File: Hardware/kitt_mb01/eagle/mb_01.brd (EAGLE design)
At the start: 160 x 100 mm, 58 parts, among them CON1 ARDUINO_UNO, IC2.00 BQ24266RGET, P1 JST.S2B-PH-SM4-TB

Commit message: entered motor controller circuitry
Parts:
- removed C1: 470uF, rcl:SMC_P
- removed C2: 390uF, rcl:SMC_P
- removed D2: MBRS320T3, diode:SMC
- removed L1: (no value), inductor-neosid:SM-B5
- removed LED1: (no value), led:PLCC2
- removed TP1: TPSQTP19SQ, testpad:TP19SQ
- removed X1: (no value), con-phoenix-254:2POL254
- added C1.01: 22uF/25V, rcl:C1210K
- added C1.02: 100nF, rcl:C0402K
- added C1.04: XX, rcl:C0402K
- added C1.05, C1.06: 22uF/6.3V, rcl:C1206K
- added C4.01: 47uF/25V, rcl:C/6032-28R
- added C4.02: 100nF/25V, resistor:C0603K
- added C4.03: (no value), resistor:C0805K
- added C4.04, C4.05: 220nF/25V, rcl:C0603K
- added IC1: (no value), kitt.ic:HSOP8
- added IC1.01: RT8293A, kitt.ic:SOIC-8-PAD
- added L2.01: 2.6uH, rcl:POWER-CHOKE_WE-TPC
- added L4.01: BEAD, inductors:0402
- added R1.03, R1.04: XX, rcl:R0402
- added R1.05, R1.06: [0R], rcl:R0402
- added R4.01, R4.02: [0R], rcl:M0805
- added R4.03: 22kR, resistor:R0402
- added R4.04, R4.05: 1kR, resistor:R0402
- added RAILS, SOC, SOC1: (no value), con-phoenix-254:2POL254
- C1.03: value [*a]1uF -> 100nF; device rcl:C0805K -> rcl:C0402K
- L1.01: value 22uH -> BEAD; device rcl:POWER-CHOKE_WE-TPC -> inductors:0402
- L1.02: value 2.6uH -> 4.7uH
- L2: value (none) -> BEAD
- R1.01: value <1>??R -> 100kR; device rcl:R0805 -> rcl:R0402
- R1.02: value <2>??R -> XX; device rcl:R0805 -> rcl:R0402
- moved R1.02 45.1 mm to (72.4, 38.1)
- moved L1.02 42.7 mm to (89.3, 56.2), turned to 270 degrees
- moved R1.01 41.4 mm to (71.1, 40.0)
- moved R3 34.0 mm to (140.6, 20.3)
- moved C1.03 26.2 mm to (87.0, 51.4), turned to 90 degrees
- moved F1 23.8 mm to (97.1, 39.7), turned to 90 degrees
- moved R2 21.9 mm to (129.8, 21.9)
- moved D1 20.8 mm to (96.9, 30.9)
- moved L1.01 7.61 mm to (113.0, 40.8), turned to 90 degrees
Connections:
- net ARDUINO.SCL renamed SCL
- net ARDUINO.SDA renamed SDA
- net AU.!IRQ_GYRO renamed !IRQ_GYRO
- new net MOT.IN1: CON1.IO.3, IC1.3, R4.05.2
- new net MOT.IN2: CON1.IO.4, IC1.2, R4.04.2
- new net N$25: C1.04.1, IC1.01.6
- new net N$28: IC1.01.5, R1.03.1, R1.04.2
- new net N$29: C1.05.1, C1.06.1, L1.02.1, L2.1, R1.03.2
- new net N$30: C1.03.2, IC1.01.3, L1.02.2
- new net N$31: C1.03.1, IC1.01.1
- new net N$32: L2.2, R1.05.2, R1.06.1
- new net N$33: C4.04.2, C4.05.1, IC1.7, SOC1.1
- new net N$34: IC1.5, R4.02.2
- new net N$35: IC1.4, R4.03.2
- net +12V: now also C4.03.1, L4.01.2, R2.1
- net +4.1V: no longer R2.04.1
- net +5V: now also IC2.00.18, IC2.00.19, R1.05.1, R1.06.2, R2.02.2, SOC.1; no longer L2.2
- net GND: now also C1.01.2, C1.02.2, C1.05.2, C1.06.2, C4.01.-, C4.02.2, C4.03.2, C4.05.2, IC1.01.4, IC1.01.PAD, IC1.1, IC1.6, IC1.THERMAL, R1.02.1, R1.04.1, R4.01.1, R4.03.1, R4.04.1, R4.05.1, SOC.2; no longer C1.-, C1.03.2, C2.-, D2.A, R1.01.1
- net GNDA: now also RAILS.2; no longer X1.2
- net N$10: now also C4.01.+, C4.02.1, C4.04.1, IC1.8, L4.01.1; no longer LED1.C, R2.1
- net N$12: now also L2.01.2; no longer L1.02.2
- net N$18: now also L2.01.1; no longer L1.02.1
- net N$2: now also L1.01.1; no longer L1.1
- net N$3: now also C1.01.1, IC1.01.2, L1.01.2, R1.01.1; no longer C1.+, L1.2
- net N$4: now also IC1.01.7; no longer R1.02.1, TP1.TP
- net N$5: now also C1.02.1, IC1.01.8; no longer D2.C, L1.01.2
- net N$7: now also C1.04.2; no longer C2.+, L1.01.1, L2.1
- net N$9: now also R4.01.2, R4.02.1, SOC1.2; no longer IC2.00.18, IC2.00.19, R2.02.2
- net V+: now also R2.04.1
- net VCC/2: now also RAILS.1; no longer LED1.A, X1.1
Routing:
- net GND: track 84.8 -> 53.6 mm
- net N$7: track 17.3 -> 0.00 mm
- net N$5: track 16.5 -> 0.00 mm
- net VCC/2: track 13.9 -> 0.00 mm
- net +12V: track 8.39 -> 0.00 mm
- net N$3: track 6.33 -> 0.00 mm
- net N$2: track 5.61 -> 0.00 mm
- net N$4: track 5.61 -> 0.00 mm
- net RAILS.RX: track 4.36 -> 0.00 mm
- net GNDA: track 3.99 -> 0.00 mm
- net N$10: track 3.28 -> 0.00 mm
- net N$9: track 1.91 -> 0.00 mm
- net +5V: track 0.00 -> 1.91 mm
- net +4.1V: track 34.2 -> 32.5 mm
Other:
- outline, holes or cut-outs redrawn

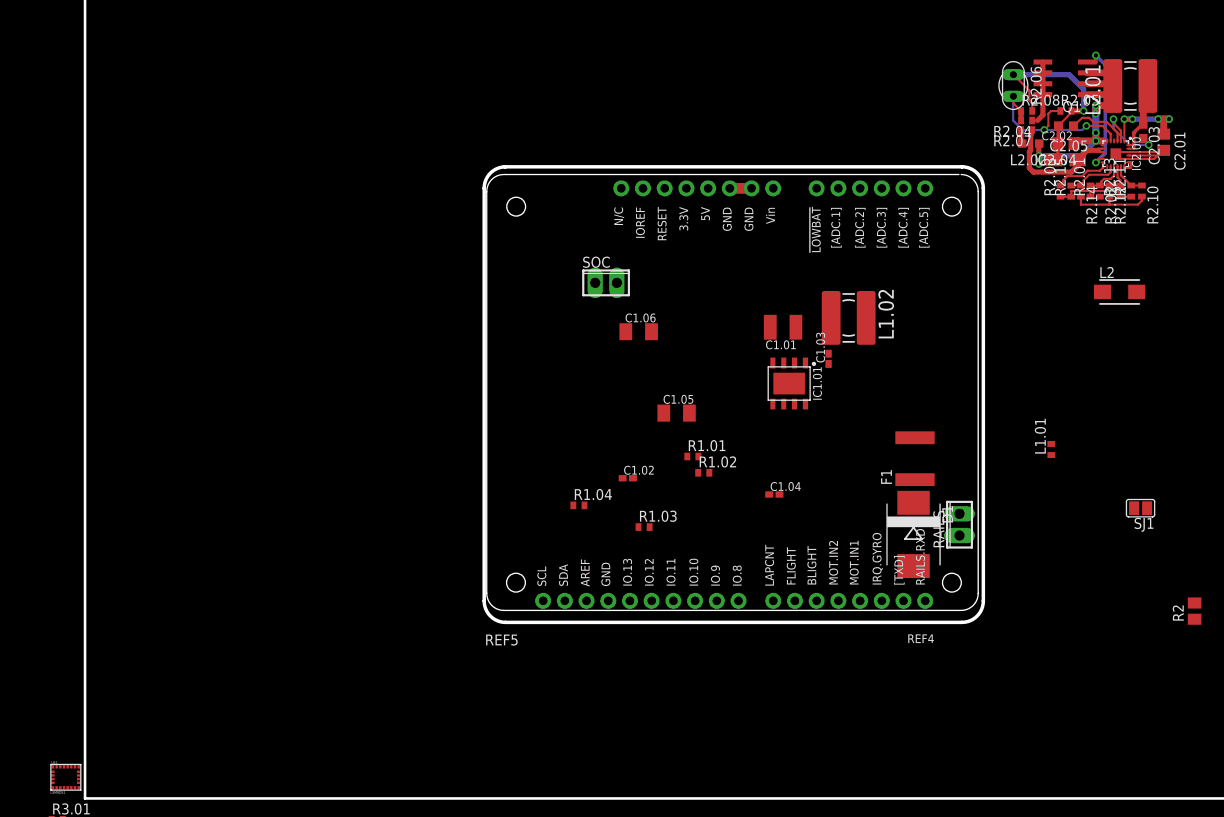
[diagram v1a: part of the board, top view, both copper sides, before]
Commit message: began working on the fullbridge
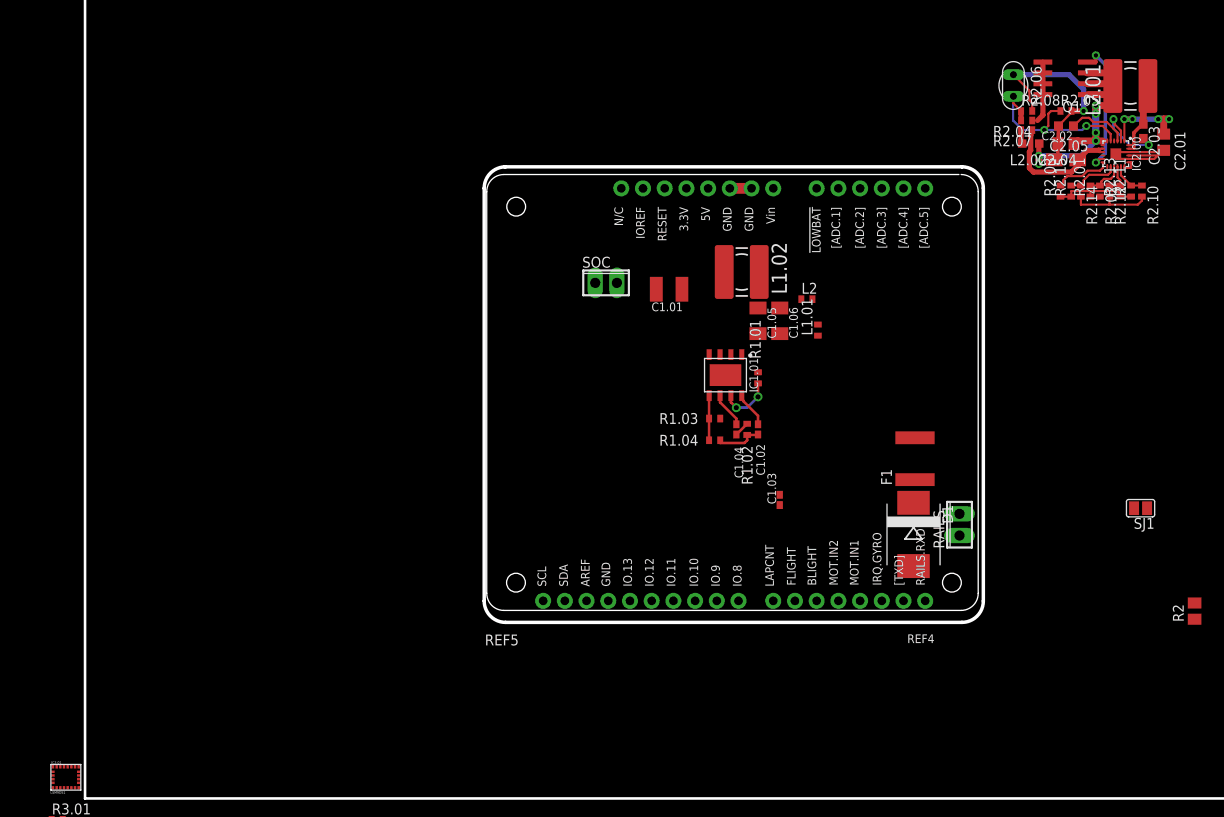
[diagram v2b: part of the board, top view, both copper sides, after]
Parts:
- L2: device inductor-neosid:SM-B5 -> inductors:0402
- moved L2 36.6 mm to (84.5, 58.4)
- moved L1.01 30.7 mm to (85.7, 54.8)
- moved R1.04 17.6 mm to (73.7, 41.9), turned to 180 degrees
- moved C1.03 17.5 mm to (81.3, 34.9)
- moved C1.06 16.6 mm to (81.3, 55.9), turned to 270 degrees
- moved C1.02 16.3 mm to (78.7, 43.2), turned to 270 degrees
- moved R1.03 15.1 mm to (73.7, 44.5)
- moved C1.05 14.4 mm to (78.7, 55.9), turned to 270 degrees
- moved C1.01 14.1 mm to (68.3, 59.6)
- moved L1.02 13.6 mm to (76.8, 61.6)
- moved R1.01 12.0 mm to (78.7, 49.2), turned to 270 degrees
- moved C1.04 8.82 mm to (76.2, 43.2), turned to 270 degrees
- moved IC1.01 7.51 mm to (74.9, 49.5)
- moved R1.02 7.18 mm to (77.5, 43.2), turned to 90 degrees
- renumbered U$1 to IC3.01
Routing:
- net N$4: track 0.00 -> 6.31 mm, vias 0 -> 2
- net GND: track 53.6 -> 59.2 mm
- net N$28: track 0.00 -> 5.24 mm
- net N$25: track 0.00 -> 4.14 mm
- net N$5: track 0.00 -> 4.09 mm
- net N$7: track 0.00 -> 1.78 mm

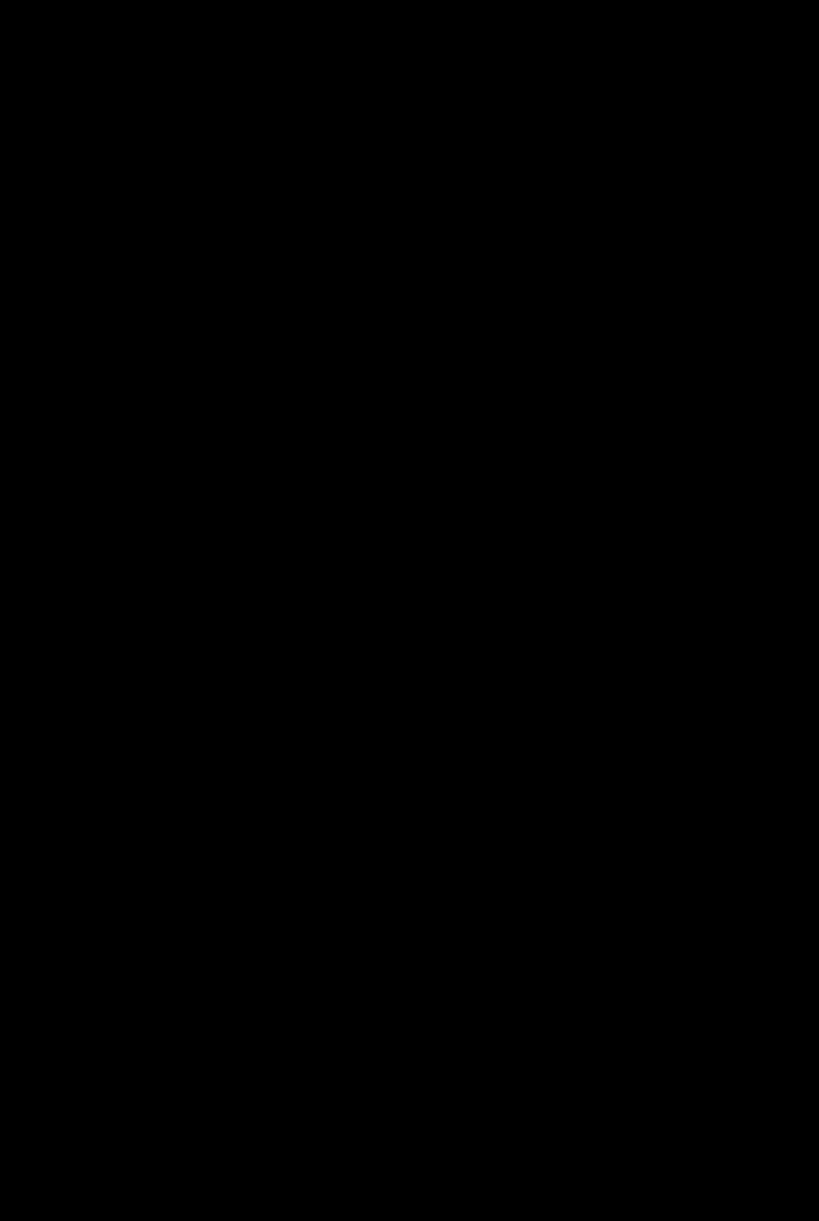
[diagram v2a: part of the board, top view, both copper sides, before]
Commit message: Alternative 5V Power Supply added (mb_01.sch)
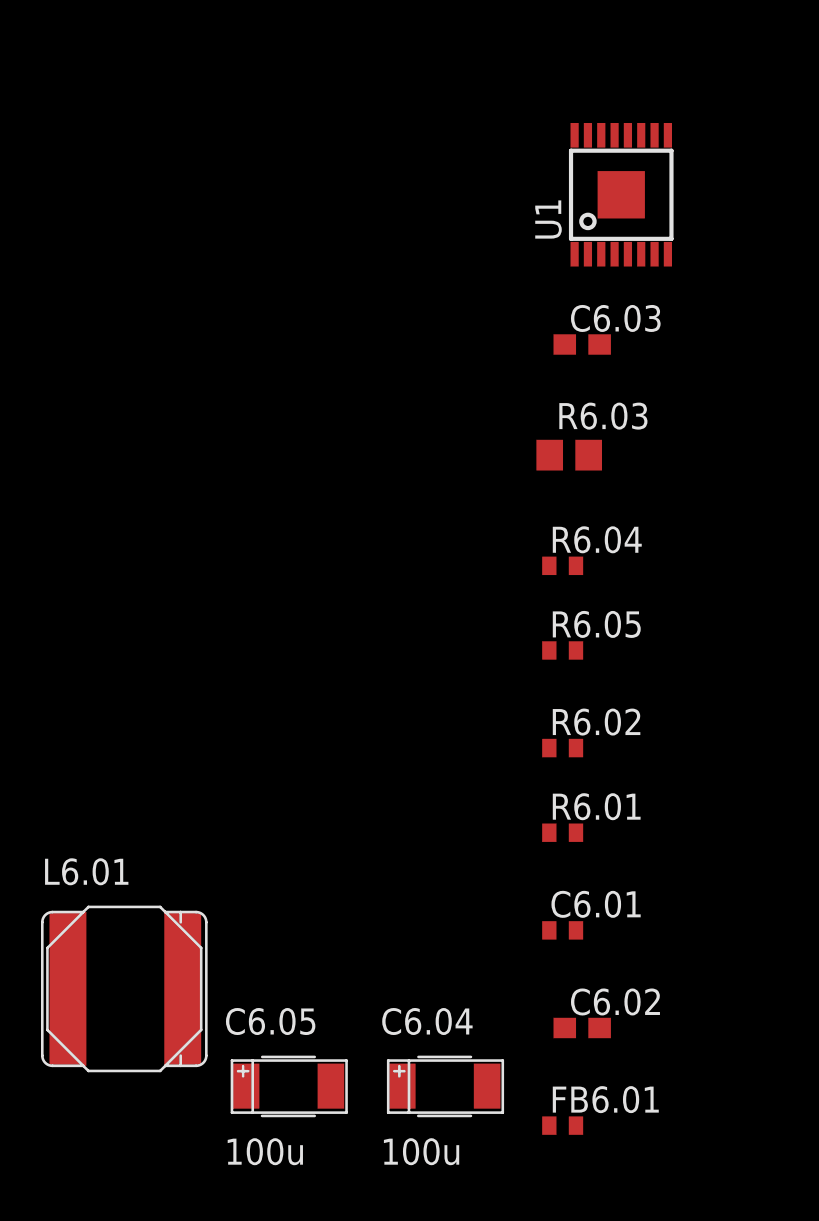
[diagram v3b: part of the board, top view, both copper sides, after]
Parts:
- added C6.01: 100n, rcl:C0402
- added C6.02: 10u, rcl:C0603
- added C6.03: 2.2uF, rcl:C0603
- added C6.04, C6.05: 100u, kitt.psvs:C-2312
- added FB6.01: BEAD, inductors:0402
- added L6.01: NRS8030XX, kitt.psvs:TAIYO-YUDEN.NRS8030T4R7MJGJ
- added R6.01: 90k9, rcl:R0402
- added R6.02, R6.04, R6.05: 100k, rcl:R0402
- added R6.03: 0R02, rcl:R0805
- added U1: TPS61032RSARPSDO-G16, kitt.ic:R-PDSO-G16
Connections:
- new net LBO: CON1.ADC.0, R6.04.1, U1.10
- new net N$36: FB6.01.2, R6.03.2
- new net N$37: R6.05.1, U1.9
- new net N$39: L6.01.2, U1.1, U1.2
- new net N$40: R6.01.2, U1.7
- new net N$41: R6.02.2, U1.8
- new net N$43: C6.03.1, C6.04.P, C6.05.P, FB6.01.1, U1.13, U1.14, U1.15
- net +3V3: now also R6.04.2
- net +4.1V: now also C6.01.1, C6.02.1, L6.01.1, R6.02.1, R6.05.2, U1.6
- net +5V: now also R6.03.1
- net GND: now also C6.01.2, C6.03.2, C6.04.N, C6.05.N, R6.01.1, U1.11, U1.5, U1.PAD

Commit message: moved merged layout to main directory and deleted garbage
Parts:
- removed D1: MBRS320T3, diode:SMC
- removed F1: 750mA, fuse:MF-SMDF050
- removed IC1: (no value), kitt.ic:HSOP8
- removed L1.01, L4.01: BEAD, inductors:0402
- removed L2.02: BEAD, rcl:L2012C
- removed P1: JST.S2B-PH-SM4-TB, kitt.con:JST_S2B-PH-SM4-TB(LF)(SN)
- removed Q1: (no value), transistor-power:SO-08
- removed R2: 10kR, rcl:M0805
- removed R2.06: 10kR/NTC, ptc-ntc:P642
- removed R3: 2k2R, rcl:M0805
- removed R4.01, R4.02: [0R], rcl:M0805
- removed RAILS, SOC, SOC1: (no value), con-phoenix-254:2POL254
- removed SJ1: (no value), jumper:SJ
- removed U1: TPS61032RSARPSDO-G16, kitt.ic:R-PDSO-G16
- added D1.01: MBRS320T3, diode:SMC
- added D7.03, D7.04: (no value), led:CHIPLED_1206
- added D7.05: OK+5V, led:CHIPLED_1206
- added D7.06: OK+3V, led:CHIPLED_1206
- added D7.07: OK+12V, led:CHIPLED_1206
- added F1.01: 750mA, rcl:R1210
- added FB1.01, FB1.02, FB2.01, FB4.01: BEAD, rcl:L4516C
- added IC4.01: (no value), kitt.ic:HSOP8
- added J4.01: (no value), jumper:SJ_2
- added NTC+, NTC-: (no value), wirepad:SMD1,27-2,54
- added Q2.01: (no value), transistor-power:SO-08
- added R7,01, R7,02, R7,04, R7,05, R7.01, R7.04, R7.08, R7.10: 330R, rcl:R0603
- added R7.02: 10kR, rcl:M0805
- added R7.03: 2k2R, rcl:M0805
- added R7.05, R7.06, R7.07: [0R], jumper:SJ
- added R7.09: [0R], rcl:R0603
- added R7.11, R7.12: SHUNT, rcl:R1206
- added REF2: REF.LOGO.UASUA, kitt.refs:REF_LOGO_UASUA
- added U$3: (no value), frames:A4L-LOC
- added U$5: (no value), marks:PASS-ROUND
- added U$8: (no value), marks:PASSER-CIRCLE
- added U6.01: TPS61032RSARPSDO-G16, kitt.ic:R-PDSO-G16
- added U7.01, U7.03, U7.2: SI1922EDH, kitt.ic:SC70-6
- added X2.01: S2B-PH-K-S(LF)(SN), kitt.con:JST_S2B-PH-K-S(LF)(SN)
- added X7.01, X7.04: (no value), con-phoenix-254:2POL254
- added X7.03, X7.06, X7.08, X7.11: CON_HEADER_1X02, kitt.con:M1X2_MALE_RIGHT_ANGLED_SMD
- added X7.05: MOTOR, con-phoenix-254:2POL254
- added X7.07: (no value), pinhead:2X03/90
- added X7.09, X7.10: 0R-JUMPA, jump-0r-smd:A0R-JMP
- C1.04: value XX -> 3.3nF
- C3.01: device rcl:C0402 -> rcl:C0603
- C3.03, C3.05: value 10nF -> 100nF
- C3.04: device rcl:C0603K -> resistor:C0603K
- C4.03: value (none) -> 4.7uF
- FB6.01: device inductors:0402 -> rcl:L4516C
- L1.02: value 4.7uH -> 15uH; device rcl:POWER-CHOKE_WE-TPC -> kitt.psvs:TAIYO-YUDEN.NRS8030T4R7MJGJ
- L2: value BEAD -> (none); device inductors:0402 -> rcl:L4516C
- L2.01: device rcl:POWER-CHOKE_WE-TPC -> kitt.psvs:TAIYO-YUDEN.NRS8030T4R7MJGJ
- R1.02: value XX -> 20kR
- R1.03: value XX -> 62kR
- R1.04: value XX -> 11.8kR
- moved C6.05 314.7 mm to (62.1, 58.6), turned to 270 degrees
- moved FB6.01 314.4 mm to (60.3, 62.7), turned to 180 degrees
- moved C6.04 310.3 mm to (58.6, 58.6), turned to 270 degrees
- moved L6.01 305.5 mm to (60.5, 50.0), turned to 180 degrees
- moved C6.02 302.7 mm to (66.0, 52.9), turned to 90 degrees
- moved C6.01 300.9 mm to (70.1, 53.5), turned to 90 degrees
- moved R6.05 298.1 mm to (69.7, 64.2), turned to 90 degrees
- moved R6.01 296.1 mm to (68.9, 53.5), turned to 90 degrees
- moved R6.02 295.8 mm to (71.0, 56.4), turned to 180 degrees
- moved R6.04 293.9 mm to (68.6, 64.2), turned to 90 degrees
- moved R6.03 285.7 mm to (59.3, 64.9)
- moved C6.03 281.7 mm to (65.9, 63.3)
- moved R4.05 240.4 mm to (65.6, 29.5), turned to 180 degrees
- moved R4.04 234.5 mm to (62.5, 29.5)
- moved R4.03 232.6 mm to (68.6, 29.5), turned to 180 degrees
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- renumbered CON1 to X7.02
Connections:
- new net ARDUINO.SCL: IC3.01.2
- new net ARDUINO.SDA: IC3.01.4
- new net CAR.AUXILLARY: U7.2.2, X7.02.IO.10
- new net CAR.BLIGHT: U7.2.5, X7.02.IO.5
- new net CAR.FLIGHT: U7.01.2, X7.02.IO.6
- new net CAR.GATECTLR: U7.01.5, X7.02.IO.9
- new net CAR.LAPCNT: X7.02.IO.7, X7.07.1
- new net CAR.SPEED: X7.02.IO.8, X7.07.2
- new net N$25: R7.11.1, X7.04.2
- new net N$28: D7.03.C, U7.03.6
- new net N$30: D7.04.A, R7.01.1
- new net N$31: D7.04.C, U7.03.3
- new net N$38: D7.06.A, R7,04.1
- new net N$4: R7.06.2, X7.02.5V
- new net N$42: R7.04.2, X7.08.1
- new net N$44: D7.07.A, R7,05.1
- new net N$45: X7.08.2, X7.10.2, X7.11.1
- new net N$46: R7.09.2, X7.06.1
- new net N$47: R7.09.1, U7.2.3
- new net N$48: X7.03.1, X7.06.2, X7.09.2
- new net N$5: R7.07.2, X7.02.VIN
- new net N$50: R7.08.2, X7.11.2
- new net N$51: R7.10.1, U7.2.6
- new net N$52: R7.10.2, X7.03.2
- new net N$7: R7.08.1, U7.01.3
- new net N$80: F1.01.2, FB1.01.1
- new net N$81: C1.01.1, FB1.01.2, IC1.01.2, R1.01.1
- new net N$87: C1.05.1, C1.06.1, FB1.02.1, L1.02.1, R1.03.2
- new net N$90: FB1.02.2, R1.05.2, R1.06.1
- net +12V: now also D1.01.C, F1.01.1, FB4.01.2, R7,05.2, R7.02.1, R7.07.1; no longer D1.C, F1.1, L4.01.2, R2.1
- net +3V3: now also R7,01.2, R7,04.2, R7.01.2, R7.05.1, X7.07.5, X7.07.6, X7.09.1, X7.10.1
- net +4.1V: now also Q2.01.5, Q2.01.6, Q2.01.7, Q2.01.8, U6.01.6, X2.01.1; no longer P1.1, Q1.5, Q1.6, Q1.7, Q1.8, U1.6
- net +5V: now also R7,02.2, R7.06.1, X7.04.1, X7.09.3, X7.10.3; no longer SOC.1
- net GND: now also C6.02.2, D7.05.C, D7.06.C, D7.07.C, IC4.01.1, IC4.01.7, IC4.01.THERMAL, J4.01.1, NTC-.1, R7.03.2, R7.11.2, R7.12.2, U6.01.11, U6.01.3, U6.01.4, U6.01.5, U6.01.PAD, U7.01.1, U7.01.4, U7.03.1, U7.03.4, U7.2.1, U7.2.4, X2.01.2, X7.07.3, X7.07.4; no longer IC1.1, IC1.6, IC1.THERMAL, P1.2, R2.06.1, R3.2, R4.01.1, SJ1.2, SOC.2, U1.11, U1.5, U1.PAD
- net GNDA: now also R7.12.1, X7.01.1; no longer RAILS.2, SJ1.1
- net IC2.0.!CHG: now also U7.03.2
- net IC2.0.!PG: now also U7.03.5
- net LBO: now also U6.01.10; no longer U1.10
- net MOT.IN1: now also IC4.01.3; no longer IC1.3
- net MOT.IN2: now also IC4.01.2; no longer IC1.2
- net N$10: now also FB4.01.1, IC4.01.5; no longer IC1.8, L4.01.1
- net N$14: now also Q2.01.4; no longer Q1.4
- net N$15: now also NTC+.1; no longer R2.06.2
- net N$16: now also FB2.01.2; no longer L2.02.2
- net N$18: now also FB2.01.1, Q2.01.1, Q2.01.2, Q2.01.3; no longer L2.02.1, Q1.1, Q1.2, Q1.3
- net N$2: now also R7.04.1, U7.01.6; no longer F1.2, L1.01.1
- net N$29: now also D7.03.A, R7,01.1; no longer C1.05.1, C1.06.1, L1.02.1, L2.1, R1.03.2
- net N$3: now also R7.05.2, X7.02.3.3V; no longer C1.01.1, IC1.01.2, L1.01.2, R1.01.1
- net N$32: now also D7.05.A, R7,02.1; no longer L2.2, R1.05.2, R1.06.1
- net N$33: now also IC4.01.6, X7.05.1; no longer IC1.7, SOC1.1
- net N$34: now also IC4.01.8, J4.01.3; no longer IC1.5, R4.02.2
- net N$35: now also IC4.01.4; no longer IC1.4
- net N$37: now also U6.01.9; no longer U1.9
- net N$39: now also U6.01.1, U6.01.2; no longer U1.1, U1.2
- net N$40: now also U6.01.7; no longer U1.7
- net N$41: now also U6.01.8; no longer U1.8
- net N$43: now also U6.01.13, U6.01.14, U6.01.15; no longer U1.13, U1.14, U1.15
- net N$9: now also J4.01.2, X7.05.2; no longer R4.01.2, R4.02.1, SOC1.2
- net RAILS.RX: now also R7.02.2, R7.03.1; no longer R2.2, R3.1
- net VCC/2: now also D1.01.A, X7.01.2; no longer D1.A, RAILS.1
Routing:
- net GND: track 59.2 -> 246.1 mm, vias 1 -> 47
- net +3V3: track 0.00 -> 161.6 mm, vias 0 -> 15
- net +5V: track 1.91 -> 151.0 mm, vias 0 -> 9
- net +12V: track 0.00 -> 104.5 mm, vias 0 -> 8
- net +4.1V: track 32.5 -> 114.7 mm, vias 0 -> 7
- net CAR.BLIGHT: track 0.00 -> 46.3 mm, vias 0 -> 4
- net CAR.GATECTLR: track 0.00 -> 40.7 mm, vias 0 -> 2
- net CAR.AUXILLARY: track 0.00 -> 40.2 mm, vias 0 -> 2
- net !IRQ_GYRO: track 0.00 -> 39.8 mm, vias 0 -> 2
- net MOT.IN1: track 0.00 -> 32.9 mm, vias 0 -> 1
- net MOT.IN2: track 0.00 -> 32.3 mm, vias 0 -> 1
- net N$87: track 0.00 -> 31.0 mm
- net CAR.LAPCNT: track 0.00 -> 30.3 mm
- net CAR.SPEED: track 0.00 -> 30.3 mm
- net CAR.FLIGHT: track 0.00 -> 30.2 mm, vias 0 -> 1
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- added copper zone on layer 16, net +4.1V
- added copper zone on layer 16, net +5V
- added copper zone on layer 3, net +5V
- added copper zone on layer 16, net CAR.FLIGHT
- added copper zone on layer 1, net GND
- added copper zone on layer 16, net GND
- added copper zone on layer 2, net GND
- added copper zone on layer 16, net N$2
- added copper zone on layer 1, net N$34
- added copper zone on layer 1, net N$39
- added copper zone on layer 1, net N$43
- added copper zone on layer 16, net N$7
- added copper zone on layer 3, net N$88
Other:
- outline, holes or cut-outs redrawn
- board text added: "+"
- board text added: "+3V3"
- board text added: "+5V"
- board text added: "<-- Battery Pak"
- board text added: "<-- Gate Control IR"
- board text added: "<-- Head Light"
- board text added: "AUX OUT -->"
- board text added: "D.Hoeginger/A.Gessler"
- board text added: "EXT.PTC"
- board text added: "GROUND POURS"
- board text added: "KITT-MB01 PCB LAYOUT"
- board text added: "Kit for Intelligent and Trainable Trackcars"
- board text added: "RAILS POURS"
- board text added: "SHUNT"
- board text added: "SPEEDBOARD --> LAPDETECTOR -->"
- board text added: "SoC Supply -->"
- board text added: "SpeedBoard--> Lap Detector-->"
- board text added: "TEST COUPON on PANELIZING -> include layer indicator and fiducial marks -> can include spare headlight -> even a I2C or decatron knightrider blinkenlight would be an option here"
- board text added: "TODO: COMMAND/BOTTOM LIGHT!!!"
- board text added: "Tail Light -->"
